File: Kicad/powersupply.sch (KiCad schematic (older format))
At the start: 19 parts, among them J801 Jack-DC, Q801 BC546, Q802 BC556, U801 DC-DC Module, U802 MAX1615, U803 TLV1117 3.3V 1A

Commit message: Fixing some review comments.
* PCB has rounded corners.
* Add JLCPCB part numbers for SMT parts
* Fixed Fab layer
* Renumbered Slots
* Mounting holes do not have thermal relief

Closes #13 #12 and #10
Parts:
- C803: LCSC Part# (none) -> C49678
- C804, C808: LCSC Part# (none) -> C15850
- C805: value 4u7 10V -> 4u7 16V; LCSC Part# (none) -> C1779
- C806: value 100n 16V -> 100n; LCSC Part# (none) -> C49678
- C807: value 1u 10V -> 1u 16V; LCSC Part# (none) -> C28323
- R801, R802, R803: LCSC Part# (none) -> C17414
- U802: LCSC Part# (none) -> C52770
- U803: LCSC Part# (none) -> C6186
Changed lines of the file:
@@
 F 7 "CPL" H 7525 3525 50  0001 C CNN "Manufacturer"
 F 8 "595-TLV1117LV33DCYR" H 7525 3525 50  0001 C CNN "Mouser"
+F 9 "C6186" H 7525 3525 50  0001 C CNN "LCSC Part#"
 	1    7525 3525
 	1    0    0    -1
@@
 P 7875 3775
 F 0 "C807" H 7993 3821 50  0000 L CNN
-F 1 "1u 10V" H 7993 3730 50  0000 L CNN
+F 1 "1u 16V" H 7993 3730 50  0000 L CNN
 F 2 "Capacitor_SMD:C_0805_2012Metric_Pad1.18x1.45mm_HandSolder" H 7913 3625 50  0001 C CNN
 F 3 "~" H 7875 3775 50  0001 C CNN
@@
 F 6 "CPL-CAP-X7R-0805-1UF-25V" H 7875 3775 50  0001 C CNN "MPN"
 F 7 "CPL" H 7875 3775 50  0001 C CNN "Manufacturer"
+F 8 "C28323" H 7875 3775 50  0001 C CNN "LCSC Part#"
 	1    7875 3775
 	1    0    0    -1
@@
 F 7 "Bel Fuse" H 2975 2125 50  0001 C CNN "Manufacturer"
 F 8 "530-0ZRS0200FF1E" H 2975 2125 50  0001 C CNN "Mouser"
+F 9 "~" H 2975 2125 50  0001 C CNN "LCSC Part#"
 	1    2975 2125
 	0    1    1    0
@@
 F 7 "Maxim" H 4725 3975 50  0001 C CNN "Manufacturer"
 F 8 "700-MAX1615EUKT" H 4725 3975 50  0001 C CNN "Mouser"
+F 9 "C52770" H 4725 3975 50  0001 C CNN "LCSC Part#"
 	1    4725 3975
 	1    0    0    -1
@@
 F 6 "CPL-CAP-X7R-0805-100NF-50V" H 4000 4275 50  0001 C CNN "MPN"
 F 7 "CPL" H 4000 4275 50  0001 C CNN "Manufacturer"
+F 8 "C49678" H 4000 4275 50  0001 C CNN "LCSC Part#"
 	1    4000 4275
 	1    0    0    -1
@@
 P 7175 3775
 F 0 "C806" H 7293 3821 50  0000 L CNN
-F 1 "100n 16V" H 7293 3730 50  0000 L CNN
+F 1 "100n" H 7293 3730 50  0000 L CNN
 F 2 "Capacitor_SMD:C_0805_2012Metric_Pad1.18x1.45mm_HandSolder" H 7213 3625 50  0001 C CNN
 F 3 "~" H 7175 3775 50  0001 C CNN
@@
 F 7 "CPL" H 7175 3775 50  0001 C CNN "Manufacturer"
 F 8 "" H 7175 3775 50  0001 C CNN "Mouser"
+F 9 "C49678" H 7175 3775 50  0001 C CNN "LCSC Part#"
 	1    7175 3775
 	-1   0    0    -1
@@
 F 6 "CPL-CAP-X5R-0805-10UF-16V" H 5275 2375 50  0001 C CNN "MPN"
 F 7 "CPL" H 5275 2375 50  0001 C CNN "Manufacturer"
+F 8 "C15850" H 5275 2375 50  0001 C CNN "LCSC Part#"
 	1    5275 2375
 	1    0    0    -1
@@
 F 7 "811-2042-ND" V 3475 2125 50  0001 C CNN "Digikey"
 F 8 "" H 3475 2125 50  0001 C CNN "Mouser"
+F 9 "~" H 3475 2125 50  0001 C CNN "LCSC Part#"
 	1    3475 2125
 	0    -1   -1   0
@@
 F 7 "CPL" H 3225 2375 50  0001 C CNN "Manufacturer"
 F 8 "" H 3225 2375 50  0001 C CNN "Mouser"
+F 9 "~" H 3225 2375 50  0001 C CNN "LCSC Part#"
 	1    3225 2375
 	-1   0    0    -1
@@
 F 7 "CPL" H 3725 2375 50  0001 C CNN "Manufacturer"
 F 8 "" H 3725 2375 50  0001 C CNN "Mouser"
+F 9 "~" H 3725 2375 50  0001 C CNN "LCSC Part#"
 	1    3725 2375
 	-1   0    0    -1
@@
 F 7 "CUI" H 2375 2225 50  0001 C CNN "Manufacturer"
 F 8 "490-PJ-063AH" H 2375 2225 50  0001 C CNN "Mouser"
+F 9 "~" H 2375 2225 50  0001 C CNN "LCSC Part#"
 	1    2375 2225
 	1    0    0    -1
@@
 F 6 "2725-K7805-3AR3-ND" H 4725 1975 50  0001 C CNN "Digikey"
 F 7 "K7805-3AR3" H 4725 1975 50  0001 C CNN "MPN"
+F 8 "~" H 4725 1975 50  0001 C CNN "LCSC Part#"
 	1    4725 1975
 	1    0    0    -1
@@
 P 5425 4275
 F 0 "C805" H 5543 4321 50  0000 L CNN
-F 1 "4u7 10V" H 5543 4230 50  0000 L CNN
+F 1 "4u7 16V" H 5543 4230 50  0000 L CNN
 F 2 "Capacitor_SMD:C_0805_2012Metric_Pad1.18x1.45mm_HandSolder" H 5463 4125 50  0001 C CNN
 F 3 "~" H 5425 4275 50  0001 C CNN
@@
 F 6 "CPL-CAP-X5R-0805-4.7UF-25V" H 5425 4275 50  0001 C CNN "MPN"
 F 7 "CPL" H 5425 4275 50  0001 C CNN "Manufacturer"
+F 8 "C1779" H 5425 4275 50  0001 C CNN "LCSC Part#"
 	1    5425 4275
 	1    0    0    -1
@@
 F 6 "ON Semiconductor" H 1925 5900 50  0001 C CNN "Manufacturer"
 F 7 "0" H 1925 5900 50  0001 C CNN "DNP"
+F 8 "~" H 1925 5900 50  0001 C CNN "LCSC Part#"
 	1    1925 5900
 	1    0    0    -1
@@
 F 6 "ON Semiconductor" H 2475 5550 50  0001 C CNN "Manufacturer"
 F 7 "0" H 2475 5550 50  0001 C CNN "DNP"
+F 8 "~" H 2475 5550 50  0001 C CNN "LCSC Part#"
 	1    2475 5550
 	1    0    0    1
@@
 F 6 "CPL-RES-0805-10K-0.125W" H 1550 5900 50  0001 C CNN "MPN"
 F 7 "CPL" H 1550 5900 50  0001 C CNN "Manufacturer"
+F 8 "C17414" H 1550 5900 50  0001 C CNN "LCSC Part#"
 	1    1550 5900
 	0    1    -1   0
@@
 F 6 "CPL-RES-0805-10K-0.125W" H 2025 5300 50  0001 C CNN "MPN"
 F 7 "CPL" H 2025 5300 50  0001 C CNN "Manufacturer"
+F 8 "C17414" H 2025 5300 50  0001 C CNN "LCSC Part#"
 	1    2025 5300
 	-1   0    0    -1
@@
 F 6 "CPL-RES-0805-10K-0.125W" H 2575 6150 50  0001 C CNN "MPN"
 F 7 "CPL" H 2575 6150 50  0001 C CNN "Manufacturer"
+F 8 "C17414" H 2575 6150 50  0001 C CNN "LCSC Part#"
 	1    2575 6150
 	-1   0    0    -1
@@
 F 6 "CPL-CAP-X5R-0805-10UF-16V" H 5850 2375 50  0001 C CNN "MPN"
 F 7 "CPL" H 5850 2375 50  0001 C CNN "Manufacturer"
+F 8 "C15850" H 5850 2375 50  0001 C CNN "LCSC Part#"
 	1    5850 2375
 	1    0    0    -1

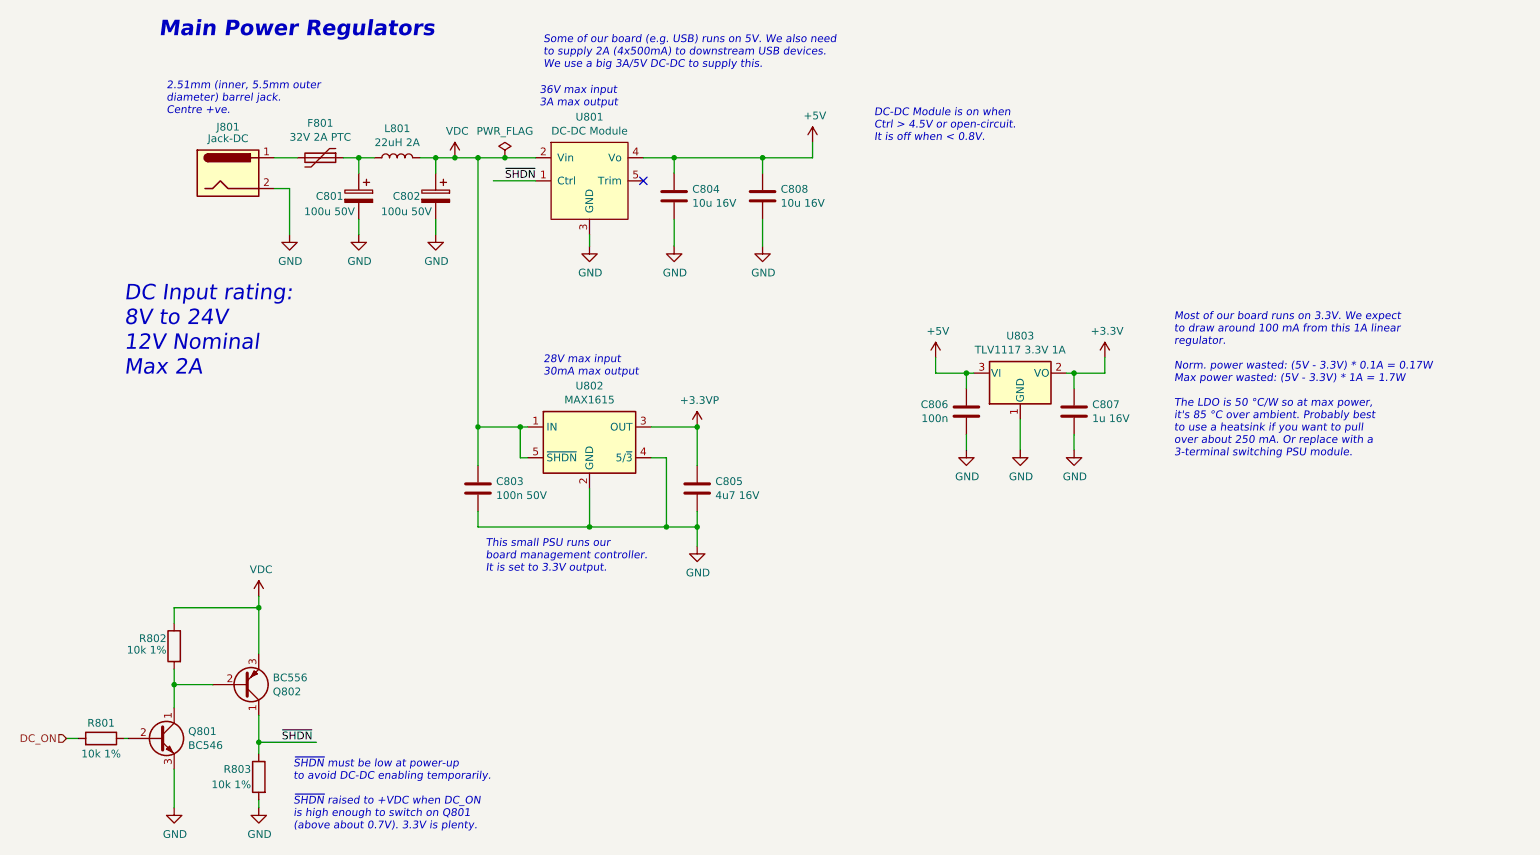
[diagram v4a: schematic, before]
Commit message: BoM and PCB fixes.
* Move tolerances and voltages out of value and into their own fields.
* Fix 5V trace for audio stage.
* Fixup docs.yml so outputs work for JLCPCB.
* Fix JLCPCB part number for 22pF caps.
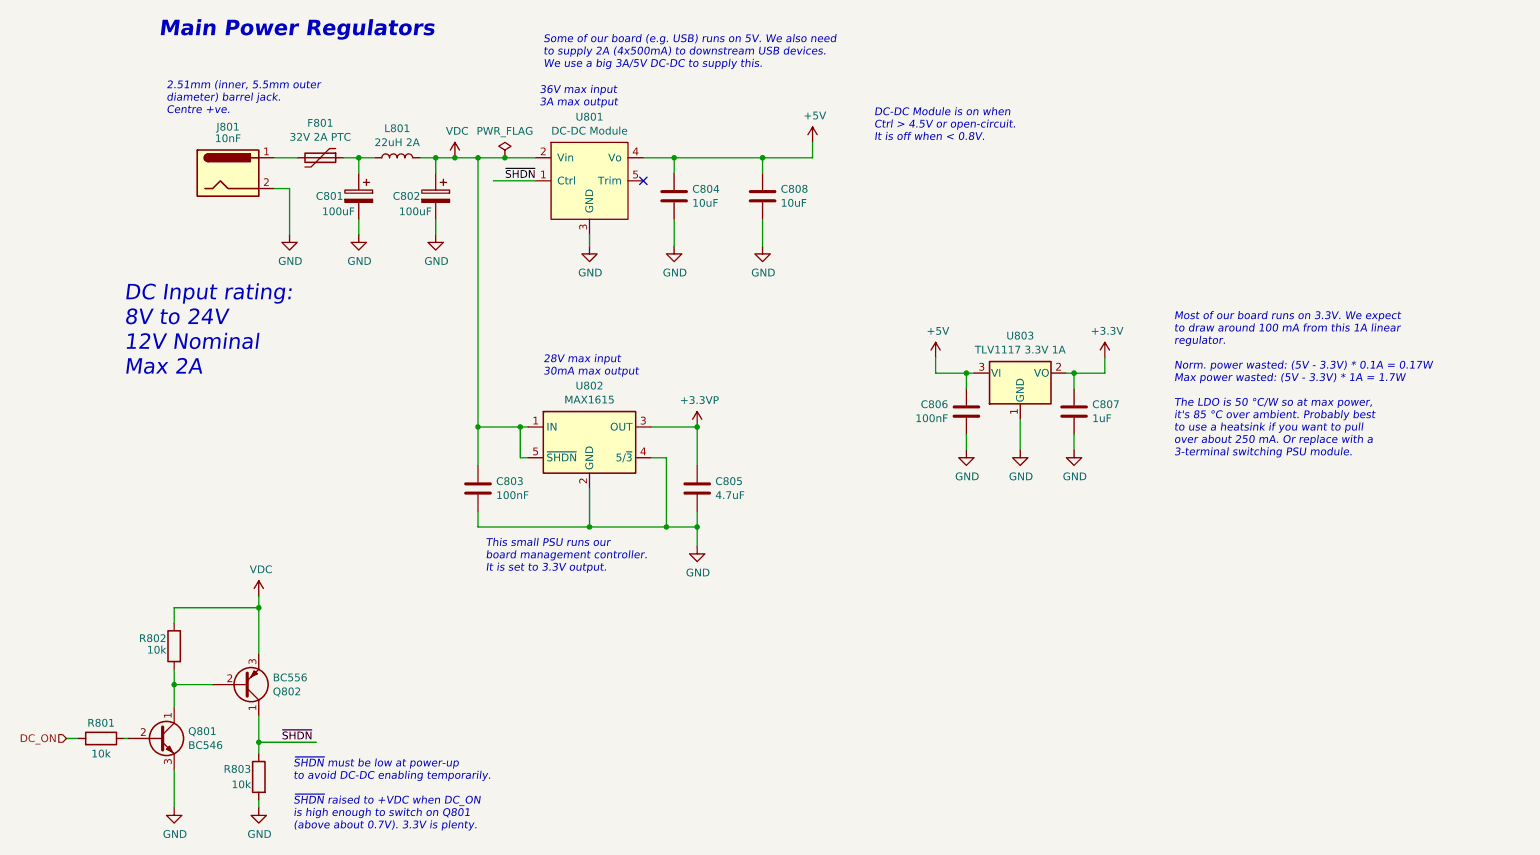
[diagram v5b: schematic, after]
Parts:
- C801, C802: value 100u 50V -> 100uF; Voltage (none) -> 50V
- C803: value 100n 50V -> 100nF; Voltage (none) -> 50V
- C804, C808: value 10u 16V -> 10uF
- C805: value 4u7 16V -> 4.7uF
- C806: value 100n -> 100nF
- C807: value 1u 16V -> 1uF
- J801: value Jack-DC -> 10nF
- R801, R802, R803: value 10k 1% -> 10k
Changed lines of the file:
@@
 P 7875 3775
 F 0 "C807" H 7993 3821 50  0000 L CNN
-F 1 "1u 16V" H 7993 3730 50  0000 L CNN
+F 1 "1uF" H 7993 3730 50  0000 L CNN
 F 2 "Capacitor_SMD:C_0805_2012Metric_Pad1.18x1.45mm_HandSolder" H 7913 3625 50  0001 C CNN
 F 3 "~" H 7875 3775 50  0001 C CNN
@@
 P 4000 4275
 F 0 "C803" H 4118 4321 50  0000 L CNN
-F 1 "100n 50V" H 4118 4230 50  0000 L CNN
+F 1 "100nF" H 4118 4230 50  0000 L CNN
 F 2 "Capacitor_SMD:C_0805_2012Metric_Pad1.18x1.45mm_HandSolder" H 4038 4125 50  0001 C CNN
 F 3 "~" H 4000 4275 50  0001 C CNN
@@
 F 7 "CPL" H 4000 4275 50  0001 C CNN "Manufacturer"
 F 8 "C49678" H 4000 4275 50  0001 C CNN "LCSC Part#"
+F 9 "50V" H 4000 4275 50  0001 C CNN "Voltage"
 	1    4000 4275
 	1    0    0    -1
@@
 P 7175 3775
 F 0 "C806" H 7293 3821 50  0000 L CNN
-F 1 "100n" H 7293 3730 50  0000 L CNN
+F 1 "100nF" H 7293 3730 50  0000 L CNN
 F 2 "Capacitor_SMD:C_0805_2012Metric_Pad1.18x1.45mm_HandSolder" H 7213 3625 50  0001 C CNN
 F 3 "~" H 7175 3775 50  0001 C CNN
@@
 P 5275 2375
 F 0 "C804" H 5393 2421 50  0000 L CNN
-F 1 "10u 16V" H 5393 2330 50  0000 L CNN
+F 1 "10uF" H 5393 2330 50  0000 L CNN
 F 2 "Capacitor_SMD:C_0805_2012Metric_Pad1.18x1.45mm_HandSolder" H 5313 2225 50  0001 C CNN
 F 3 "~" H 5275 2375 50  0001 C CNN
@@
 P 3225 2375
 F 0 "C801" H 3325 2375 50  0000 L CNN
-F 1 "100u 50V" H 3250 2275 50  0000 L CNN
+F 1 "100uF" H 3250 2275 50  0000 L CNN
 F 2 "Capacitor_THT:CP_Radial_D6.3mm_P2.50mm" H 3263 2225 50  0001 C CNN
 F 3 "~" H 3225 2375 50  0001 C CNN
@@
 F 8 "" H 3225 2375 50  0001 C CNN "Mouser"
 F 9 "~" H 3225 2375 50  0001 C CNN "LCSC Part#"
+F 10 "50V" H 3225 2375 50  0001 C CNN "Voltage"
 	1    3225 2375
 	-1   0    0    -1
@@
 P 3725 2375
 F 0 "C802" H 3825 2375 50  0000 L CNN
-F 1 "100u 50V" H 3750 2275 50  0000 L CNN
+F 1 "100uF" H 3750 2275 50  0000 L CNN
 F 2 "Capacitor_THT:CP_Radial_D6.3mm_P2.50mm" H 3763 2225 50  0001 C CNN
 F 3 "~" H 3725 2375 50  0001 C CNN
@@
 F 8 "" H 3725 2375 50  0001 C CNN "Mouser"
 F 9 "~" H 3725 2375 50  0001 C CNN "LCSC Part#"
+F 10 "50V" H 3725 2375 50  0001 C CNN "Voltage"
 	1    3725 2375
 	-1   0    0    -1
@@
 P 2375 2225
 F 0 "J801" H 2375 2525 50  0000 C CNN
-F 1 "Jack-DC" H 2375 2450 50  0000 C CNN
+F 1 "10nF" H 2375 2450 50  0000 C CNN
 F 2 "Connector_BarrelJack:BarrelJack_CUI_PJ-063AH_Horizontal" H 2425 2185 50  0001 C CNN
 F 3 "~" H 2425 2185 50  0001 C CNN
@@
 P 5425 4275
 F 0 "C805" H 5543 4321 50  0000 L CNN
-F 1 "4u7 16V" H 5543 4230 50  0000 L CNN
+F 1 "4.7uF" H 5543 4230 50  0000 L CNN
 F 2 "Capacitor_SMD:C_0805_2012Metric_Pad1.18x1.45mm_HandSolder" H 5463 4125 50  0001 C CNN
 F 3 "~" H 5425 4275 50  0001 C CNN
@@
 P 1550 5900
 F 0 "R801" V 1650 5900 50  0000 C CNN
-F 1 "10k 1%" V 1450 5900 50  0000 C CNN
+F 1 "10k" V 1450 5900 50  0000 C CNN
 F 2 "Resistor_SMD:R_0805_2012Metric_Pad1.20x1.40mm_HandSolder" V 1480 5900 50  0001 C CNN
 F 3 "~" H 1550 5900 50  0001 C CNN
@@
 P 2025 5300
 F 0 "R802" H 2075 5350 50  0000 L CNN
-F 1 "10k 1%" H 2075 5275 50  0000 L CNN
+F 1 "10k" H 2075 5275 50  0000 L CNN
 F 2 "Resistor_SMD:R_0805_2012Metric_Pad1.20x1.40mm_HandSolder" V 1955 5300 50  0001 C CNN
 F 3 "~" H 2025 5300 50  0001 C CNN
@@
 P 2575 6150
 F 0 "R803" H 2625 6200 50  0000 L CNN
-F 1 "10k 1%" H 2625 6100 50  0000 L CNN
+F 1 "10k" H 2625 6100 50  0000 L CNN
 F 2 "Resistor_SMD:R_0805_2012Metric_Pad1.20x1.40mm_HandSolder" V 2505 6150 50  0001 C CNN
 F 3 "~" H 2575 6150 50  0001 C CNN
@@
 P 5850 2375
 F 0 "C808" H 5968 2421 50  0000 L CNN
-F 1 "10u 16V" H 5968 2330 50  0000 L CNN
+F 1 "10uF" H 5968 2330 50  0000 L CNN
 F 2 "Capacitor_SMD:C_0805_2012Metric_Pad1.18x1.45mm_HandSolder" H 5888 2225 50  0001 C CNN
 F 3 "~" H 5850 2375 50  0001 C CNN

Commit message: Feature/swap layers (#22)
* Switch around the layers.

We now have:

1. Signal + Ground
2. Power (3.3V)
3. Ground
4. Signal + Power (3.3V)

This balances things a bit better than Sig/Gnd, Power, Ground, Sig/Gnd.

* Replace MCP7940N with DIP. Also enlarge some caps.

The capacitor footprints were just too small for such large value
electrolytics. The RTC footprint was due to availability.
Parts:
- C801, C802: footprint Capacitor_THT:CP_Radial_D6.3mm_P2.50mm -> Capacitor_THT:CP_Radial_D8.0mm_P5.00mm
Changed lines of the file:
@@
 Sheet 8 11
 Title "Neotron Common Hardware - Power Supply"
-Date "2021-06-03"
+Date "2021-06-10"
 Rev "[Uncontrolled]"
 Comp "https://neotron-compute.github.io/"
@@
 F 0 "C801" H 3325 2375 50  0000 L CNN
 F 1 "100uF" H 3250 2275 50  0000 L CNN
-F 2 "Capacitor_THT:CP_Radial_D6.3mm_P2.50mm" H 3263 2225 50  0001 C CNN
+F 2 "Capacitor_THT:CP_Radial_D8.0mm_P5.00mm" H 3263 2225 50  0001 C CNN
 F 3 "~" H 3225 2375 50  0001 C CNN
 F 4 "0" H 3225 2375 50  0001 C CNN "DNP"
@@
 F 0 "C802" H 3825 2375 50  0000 L CNN
 F 1 "100uF" H 3750 2275 50  0000 L CNN
-F 2 "Capacitor_THT:CP_Radial_D6.3mm_P2.50mm" H 3763 2225 50  0001 C CNN
+F 2 "Capacitor_THT:CP_Radial_D8.0mm_P5.00mm" H 3763 2225 50  0001 C CNN
 F 3 "~" H 3725 2375 50  0001 C CNN
 F 4 "0" H 3725 2375 50  0001 C CNN "DNP"

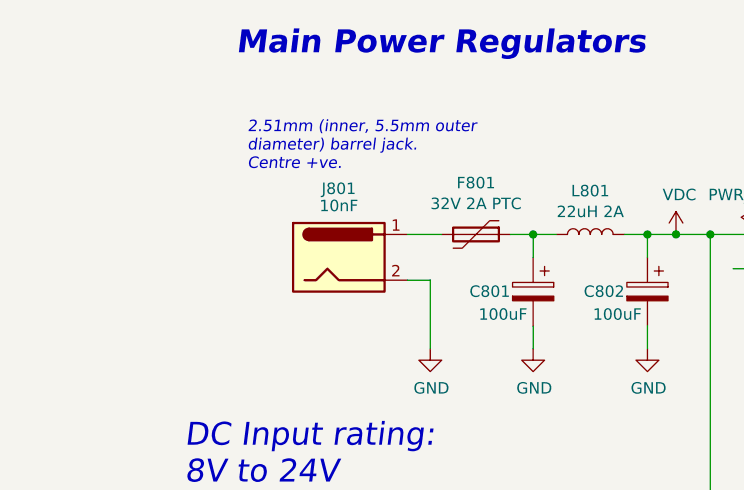
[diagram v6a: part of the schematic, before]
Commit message: Remove PS/2 SIP array and fix DC jack value. (#26)
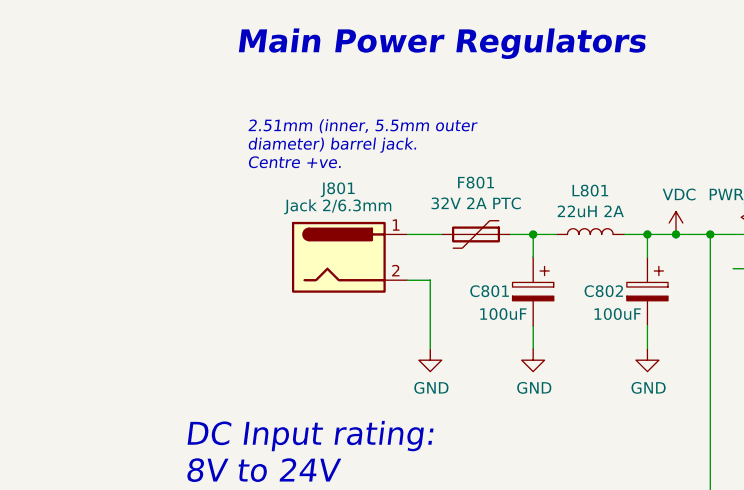
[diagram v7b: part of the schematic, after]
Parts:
- J801: value 10nF -> Jack 2/6.3mm
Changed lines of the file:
@@
 P 2375 2225
 F 0 "J801" H 2375 2525 50  0000 C CNN
-F 1 "10nF" H 2375 2450 50  0000 C CNN
+F 1 "Jack 2/6.3mm" H 2375 2450 50  0000 C CNN
 F 2 "Connector_BarrelJack:BarrelJack_CUI_PJ-063AH_Horizontal" H 2425 2185 50  0001 C CNN
 F 3 "~" H 2425 2185 50  0001 C CNN
